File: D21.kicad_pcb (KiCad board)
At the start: 6 copper layers, 15 x 9.5 mm, 48 parts, among them IC1 AVR64DD28-I_STX, IC2 NCP730BM, IC3 DRV8231ADSGR, J1 Conn_01x01, J10 Conn_02x09_Counter_Clockwise, J2 Conn_01x01, J3 Conn_01x01, Q1 BC847BDW1, Q2 BC857BDW1, Q3 PMZB200UNEYL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

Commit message: add: fuses
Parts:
- C2, C4, C7: value 22u/25V -> 10u/25V
- J1, J2, J3: value Conn_01x01 -> pad
- J10: value Conn_02x09_Counter_Clockwise -> Next18
- R13: value 3.3k -> 1k
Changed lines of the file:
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@@
   (title_block
     (title "RTB D21 Next18 Decoder")
-    (date 2024-11-15)
+    (date 2025-04-20)
     (rev 0)
     (company "Frank Schumacher")
@@
     (45 Margin user hide)
     (46 B.CrtYd user)
-    (47 F.CrtYd user hide)
+    (47 F.CrtYd user)
     (48 B.Fab user hide)
     (49 F.Fab user hide)
@@
       (effects (font (size 1.27 1.27) (thickness 0.254)) (justify mirror))
     )
-    (fp_text value SM5819L2-TP (at 0 0 180 unlocked) (layer B.Fab)
+    (fp_text value SM5819L2-TP (at -5.42 1.14 180 unlocked) (layer B.Fab)
       (effects (font (size 1.27 1.27) (thickness 0.254)) (justify mirror))
     )
@@
       (effects (font (size 1 1) (thickness 0.15)))
     )
-    (fp_text value AVR64DD28-I_STX (at 0 3.3) (layer F.Fab)
+    (fp_text value AVR64DD28-I_STX (at 4.92 3.25) (layer F.Fab)
       (effects (font (size 1 1) (thickness 0.15)))
     )
@@
       (effects (font (size 1 1) (thickness 0.15)) (justify mirror))
     )
-    (fp_text value Conn_01x01 (at 0 -1.55) (layer B.Fab) hide
+    (fp_text value pad (at 0 -1.55) (layer B.Fab) hide
       (effects (font (size 1 1) (thickness 0.15)) (justify mirror))
     )
@@
       (effects (font (size 1.27 1.27) (thickness 0.254)))
     )
-    (fp_text value Conn_02x09_Counter_Clockwise (at 0 0 90) (layer F.Fab)
+    (fp_text value Next18 (at 0 0 90) (layer F.Fab)
       (effects (font (size 1.27 1.27) (thickness 0.254)))
     )
@@
       (effects (font (size 1 1) (thickness 0.15)) (justify mirror))
     )
-    (fp_text value 22u/25V (at 0 -1.43) (layer B.Fab)
+    (fp_text value 10u/25V (at 0 -1.43) (layer B.Fab)
       (effects (font (size 1 1) (thickness 0.15)) (justify mirror))
     )
@@
       (effects (font (size 1 1) (thickness 0.15)) (justify mirror))
     )
-    (fp_text value 22u/25V (at 0 -1.43) (layer B.Fab)
+    (fp_text value 10u/25V (at 0 -1.43) (layer B.Fab)
       (effects (font (size 1 1) (thickness 0.15)) (justify mirror))
     )
@@
       (effects (font (size 1 1) (thickness 0.15)))
     )
-    (fp_text value Conn_01x01 (at 0 -1.55) (layer B.Fab) hide
+    (fp_text value pad (at 0 -1.55) (layer B.Fab) hide
       (effects (font (size 1 1) (thickness 0.15)) (justify mirror))
     )
@@
       (effects (font (size 1 1) (thickness 0.15)))
     )
-    (fp_text value Conn_01x01 (at 0 -1.55) (layer B.Fab) hide
+    (fp_text value pad (at 0 -1.55) (layer B.Fab) hide
       (effects (font (size 1 1) (thickness 0.15)) (justify mirror))
     )
@@
       (effects (font (size 1 1) (thickness 0.15)) (justify mirror))
     )
-    (fp_text value 22u/25V (at 0 -1.43) (layer B.Fab)
+    (fp_text value 10u/25V (at 0 -1.43) (layer B.Fab)
       (effects (font (size 1 1) (thickness 0.15)) (justify mirror))
     )
@@
       (effects (font (size 1 1) (thickness 0.15)))
     )
-    (fp_text value 10k (at 0 1.17 270) (layer F.Fab)
+    (fp_text value 10k (at -0.03 -0.59 270) (layer F.Fab)
       (effects (font (size 1 1) (thickness 0.15)))
     )
@@
       (effects (font (size 1 1) (thickness 0.15)) (justify mirror))
     )
-    (fp_text value 3.3k (at 0 -1.17 180) (layer B.Fab)
-      (effects (font (size 1 1) (thickness 0.15)) (justify mirror))
-    )
+    (fp_text value 1k (at 0 -1.17 180) (layer B.Fab)
+      (effects (font (size 1 1) (thickness 0.15)) (justify mirror))
+    )

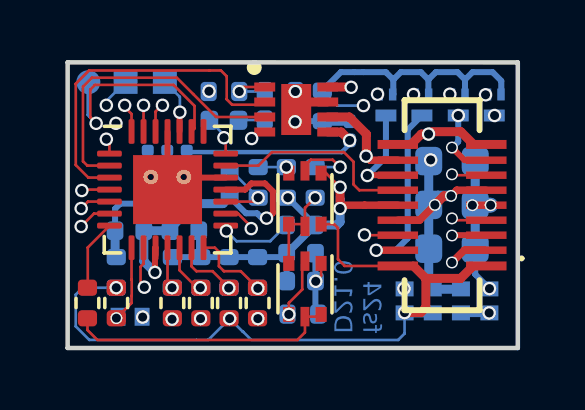
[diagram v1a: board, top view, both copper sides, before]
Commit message: updated Kicad version
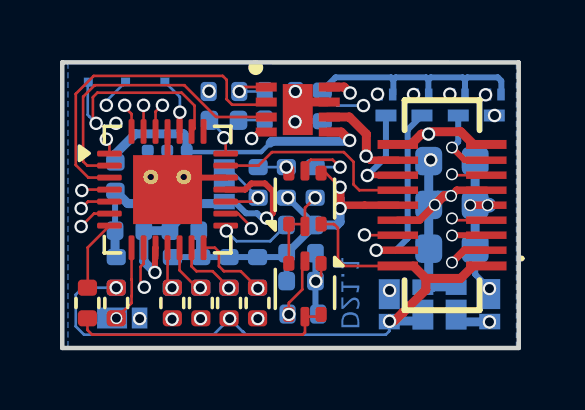
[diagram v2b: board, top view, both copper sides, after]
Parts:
- C1, C5, C8, C9: value 22u/6V -> 10u/6.3V
- C10: value 100n -> 100n/50V; footprint Capacitor_SMD:C_0201_0603Metric -> Capacitor_SMD:C_0402_1005Metric
- C6: value 1u -> 1u/50V
- D2, D3, D4, D5, D6, D7: value SM5819L2-TP -> NSR20F40NXT5G; footprint RTB:SM5819L2TP -> RTB:NSR20F40NXT5G
- IC2: value NCP730BM -> NCP730BMT500TBG
- R16, R18: value 10k -> 12k
- moved C10 7.96 mm to (54.1, -45.1), turned to -90 degrees
- moved D5 0.56 mm to (63.2, -40.8)
- moved D4 0.33 mm to (64.3, -41.0)
- moved D2 0.23 mm to (66.6, -40.8)
- moved D6 0.23 mm to (57.7, -44.8)
- moved D3 0.16 mm to (65.5, -41.0)
- moved D7 0.15 mm to (54.4, -40.4)
- moved IC3 0.05 mm to (60.2, -47.4)
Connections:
- IC1 pad 22: (no net) -> unconnected-(IC1-PF6_(~{RESET})-Pad22)
- IC2 pad 2: (no net) -> unconnected-(IC2-NC/ADJ-Pad2)
- IC2 pad 4: (no net) -> unconnected-(IC2-EN-Pad4)
- IC2 pad 5: (no net) -> unconnected-(IC2-NC/PG-Pad5)
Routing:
- net +3V3: track 15.3 -> 20.3 mm
- net VHBR: track 21.0 -> 24.2 mm
- net M1: track 19.3 -> 18.2 mm
- net DCC-a: track 24.8 -> 24.0 mm
- net aSENSE: track 26.4 -> 25.8 mm
- net M2: track 22.7 -> 22.1 mm
- net AUX1: track 17.8 -> 17.2 mm
- net Lf: vias 2 -> 1
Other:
- board size 15 x 9.5 mm -> 15.2 x 9.5 mm
- net class Default removed
- net class Power removed
- board text added: "D21.1"
- board text removed: "fs24 D21.0"
